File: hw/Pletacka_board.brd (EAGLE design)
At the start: 74.9 x 100 mm, 45 parts, among them U1 LM75BDP, U2 EL357N(A)(TA)-G, U3 EL357N(A)(TA)-G, U4 EL357N(A)(TA)-G, U5 EL357N(A)(TA)-G, U6 TPS54231D

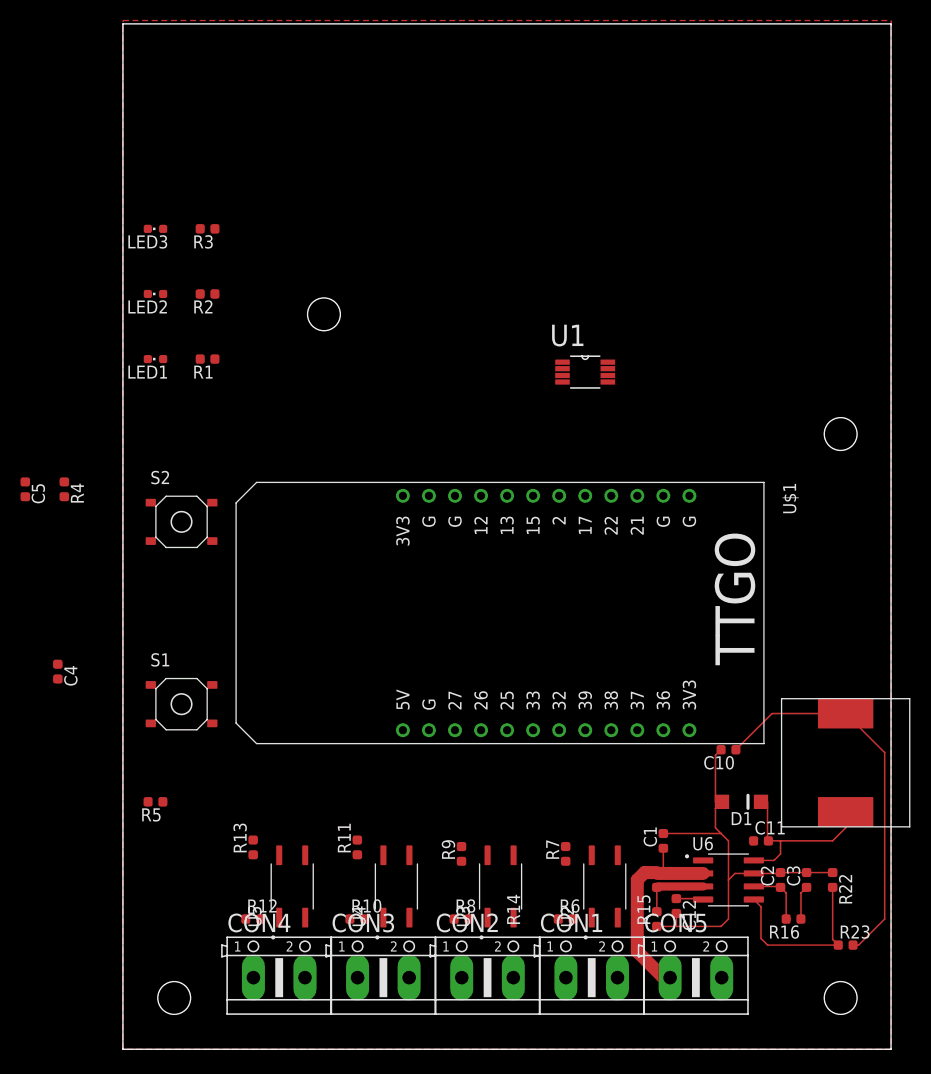
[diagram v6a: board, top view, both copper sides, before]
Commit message: Route power supply
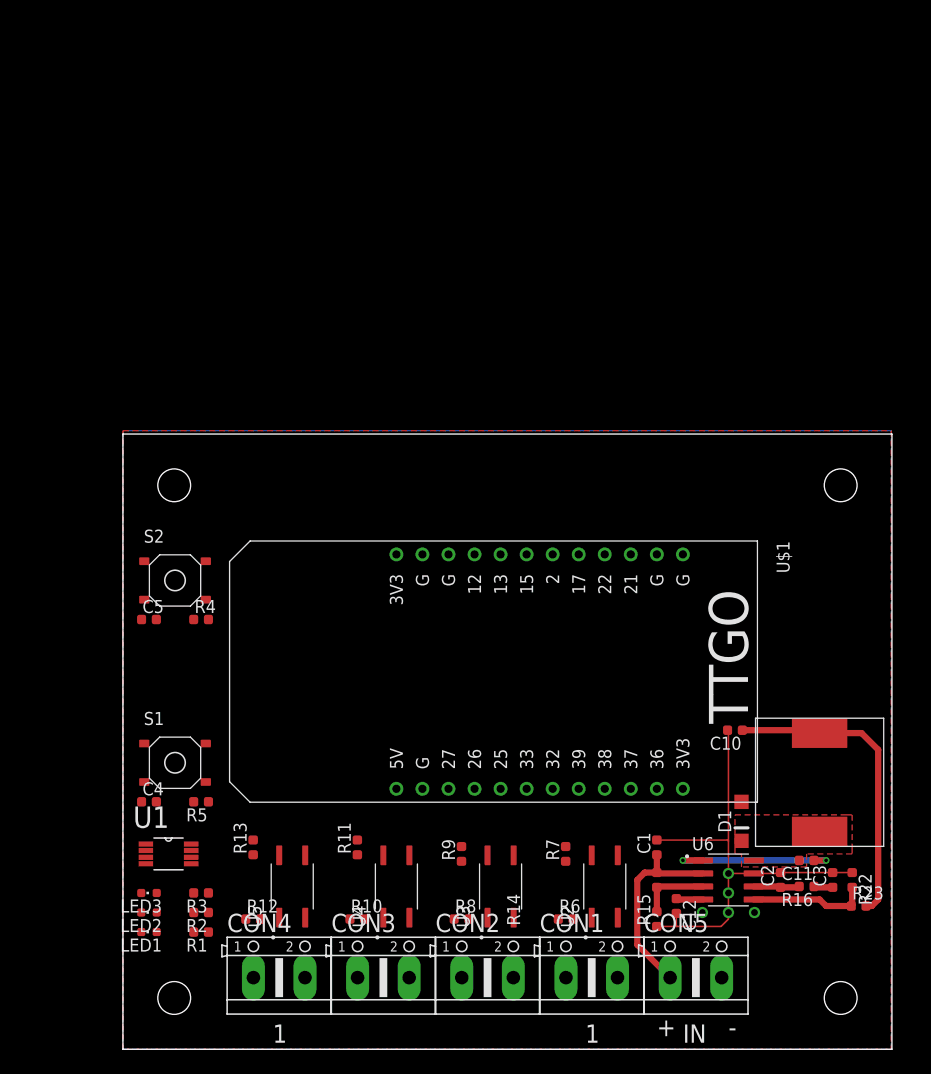
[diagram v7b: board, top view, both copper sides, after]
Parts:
- moved LED3 64.8 mm to (2.54, 15.2)
- moved R3 64.8 mm to (7.62, 15.2)
- moved U1 62.1 mm to (4.45, 19.1)
- moved LED2 60.3 mm to (2.54, 13.3)
- moved R2 60.3 mm to (7.62, 13.3)
- moved LED1 55.9 mm to (2.54, 11.4)
- moved R1 55.9 mm to (7.62, 11.4)
- moved R4 18.4 mm to (7.62, 41.9), turned to 0 degrees
- moved C5 17.5 mm to (2.54, 41.9), turned to 0 degrees
- moved C4 15.5 mm to (2.54, 24.1), turned to 0 degrees
- moved S2 5.75 mm to (5.08, 45.7)
- moved U$1 5.75 mm to (25.4, 36.8)
- moved S1 5.75 mm to (5.08, 27.9)
- moved C11 4.84 mm to (66.7, 18.4), turned to 180 degrees
- moved R5 4.45 mm to (7.62, 24.1)
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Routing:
- net BOOT: track 0.10 -> 19.1 mm, vias 0 -> 2
- net PH: track 18.2 -> 0.00 mm
- net +5V: track 37.9 -> 30.7 mm
- net VSENSE: track 17.8 -> 11.6 mm
- net GND: track 42.7 -> 47.5 mm, vias 0 -> 3
- net VIN: track 24.9 -> 21.2 mm
- net COMP: track 6.38 -> 4.50 mm
- net N$25: track 3.32 -> 1.86 mm
- added copper zone on layer 16, net GND
- added copper zone on layer 1, net PH
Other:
- board size 74.9 x 100 mm -> 75 x 60 mm
- board text added: "+"
- board text added: "-"
- board text added: "1"
- board text added: "IN"

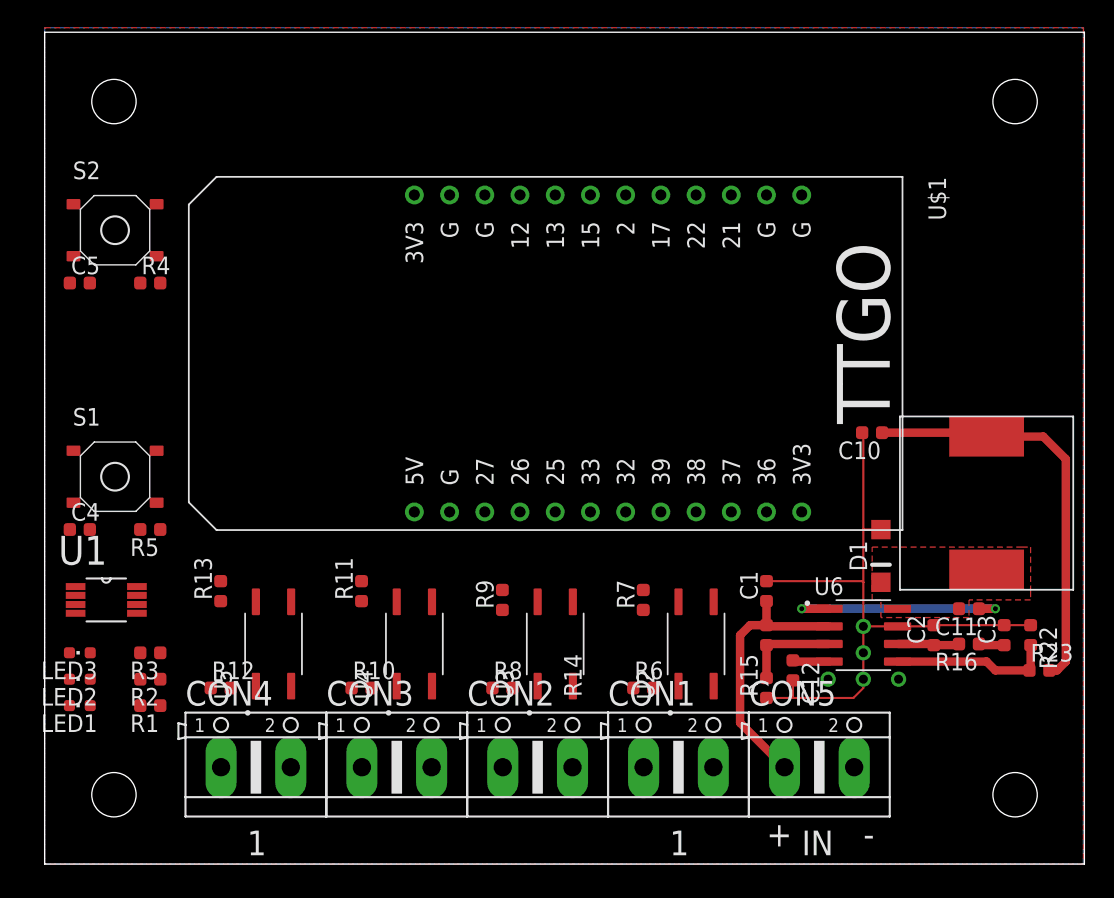
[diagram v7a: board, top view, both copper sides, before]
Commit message: Finish first routing
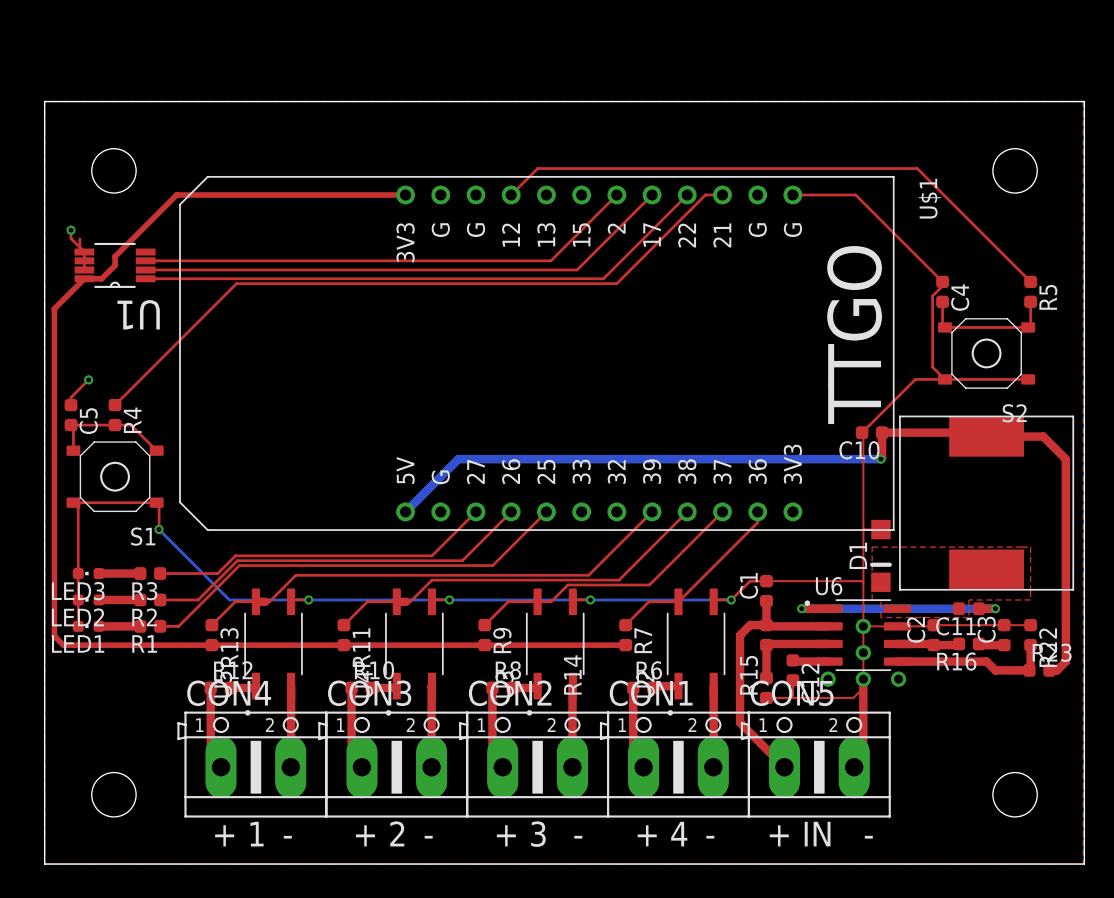
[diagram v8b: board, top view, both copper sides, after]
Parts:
- moved R5 65.8 mm to (71.1, 41.3), turned to 270 degrees
- moved C4 64.5 mm to (64.8, 41.3), turned to 270 degrees
- moved S2 63.5 mm to (67.9, 36.8), turned to 180 degrees
- moved U1 24.1 mm to (5.08, 43.2), turned to 180 degrees
- moved R4 9.86 mm to (5.08, 32.4), turned to 270 degrees
- moved C5 9.55 mm to (1.91, 32.4), turned to 270 degrees
- moved LED1 5.75 mm to (3.17, 17.1)
- moved LED2 5.75 mm to (3.17, 19.1)
- moved LED3 5.75 mm to (3.17, 21.0)
- moved R1 5.71 mm to (7.62, 17.1)
- moved R2 5.71 mm to (7.62, 19.1)
- moved R3 5.71 mm to (7.62, 21.0)
- moved R11 3.42 mm to (21.6, 16.5), turned to 270 degrees
- moved R13 3.24 mm to (12.1, 16.5), turned to 270 degrees
- moved R7 2.84 mm to (41.9, 16.5), turned to 270 degrees
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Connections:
- net RFID renamed N$3
- removed net N$3 (its old number): U$1.17
- new net N$27: U$1.13
- net BUTTON1: now also U$1.21; no longer U$1.13
- net N$4: now also U$1.33; no longer U$1.2
- net TMP_OS: now also U$1.2; no longer U$1.33
- net TMP_SCL: now also U$1.17; no longer U$1.22
- net TMP_SDA: now also U$1.22; no longer U$1.21
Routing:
- net GND: track 47.5 -> 164.9 mm, vias 3 -> 10
- net +3V3: track 0.00 -> 94.2 mm
- net BUTTON1: track 0.00 -> 50.1 mm
- net BUTTON2: track 0.00 -> 41.6 mm
- net TMP_SDA: track 0.00 -> 41.6 mm
- net TMP_SCL: track 0.00 -> 38.8 mm
- net +5V: track 30.7 -> 68.5 mm, vias 0 -> 1
- net TMP_OS: track 0.00 -> 36.0 mm
- net OPTO4: track 0.00 -> 35.8 mm
- net LED_POWER: track 0.00 -> 31.3 mm
- net OPTO3: track 0.00 -> 28.8 mm
- net LED_WIFI: track 0.00 -> 27.9 mm
- net LED_SEND: track 0.00 -> 24.6 mm
- net OPTO2: track 0.00 -> 20.5 mm
- net OPTO1: track 0.00 -> 13.4 mm
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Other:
- board size 75 x 60 mm -> 75 x 55 mm
- board text added: "2"
- board text added: "3"
- board text added: "4"
